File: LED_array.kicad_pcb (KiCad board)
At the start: 4 copper layers, 40 x 48 mm, 135 parts, among them J1 5040500691

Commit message: uodate 5/4/2021
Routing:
- net +5VD: track 109.7 -> 108.4 mm
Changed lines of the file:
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@@
     (thickness 1.6)
     (drawings 14)
-    (tracks 732)
+    (tracks 730)
     (zones 0)
     (modules 135)
@@
   (layers
     (0 F.Cu signal)
-    (1 In1.Cu power)
-    (2 In2.Cu signal)
+    (1 In1.Cu power hide)
+    (2 In2.Cu signal hide)
     (31 B.Cu power)
-    (32 B.Adhes user)
-    (33 F.Adhes user)
-    (34 B.Paste user)
-    (35 F.Paste user)
-    (36 B.SilkS user)
-    (37 F.SilkS user)
-    (38 B.Mask user)
-    (39 F.Mask user)
-    (40 Dwgs.User user)
-    (41 Cmts.User user)
-    (42 Eco1.User user)
-    (43 Eco2.User user)
-    (44 Edge.Cuts user)
-    (45 Margin user)
-    (46 B.CrtYd user)
-    (47 F.CrtYd user)
+    (32 B.Adhes user hide)
+    (33 F.Adhes user hide)
+    (34 B.Paste user hide)
+    (35 F.Paste user hide)
+    (36 B.SilkS user hide)
+    (37 F.SilkS user hide)
+    (38 B.Mask user hide)
+    (39 F.Mask user hide)
+    (40 Dwgs.User user hide)
+    (41 Cmts.User user hide)
+    (42 Eco1.User user hide)
+    (43 Eco2.User user hide)
+    (44 Edge.Cuts user hide)
+    (45 Margin user hide)
+    (46 B.CrtYd user hide)
+    (47 F.CrtYd user hide)
     (48 B.Fab user hide)
     (49 F.Fab user hide)
@@
       (effects (font (size 1 1) (thickness 0.015)))
     )
-    (fp_text user 1.50mm~Pitch,~Pico-Lock~PCB~Header,~Single~Row,~Right-Angle (at -10.5 5) (layer F.Fab)
-      (effects (font (size 0.393701 0.393701) (thickness 0.015)))
-    )
     (fp_poly (pts (xy -7.8762 -0.5762) (xy -7.1238 -0.5762) (xy -7.1238 0.5762) (xy -7.8762 0.5762)) (layer F.Mask) (width 0.01))
     (fp_poly (pts (xy -6.3762 -0.5762) (xy -5.6238 -0.5762) (xy -5.6238 0.5762) (xy -6.3762 0.5762)) (layer F.Mask) (width 0.01))
@@
     (fp_line (start 4.295 -7.36) (end 4.295 1.62) (layer F.CrtYd) (width 0.05))
     (fp_line (start -11.795 -7.36) (end 4.295 -7.36) (layer F.CrtYd) (width 0.05))
+    (fp_text user 1.50mm~Pitch,~Pico-Lock~PCB~Header,~Single~Row,~Right-Angle (at -10.5 5) (layer F.Fab)
+      (effects (font (size 0.393701 0.393701) (thickness 0.015)))
+    )
     (pad S1 smd rect (at 2.605 -5.19) (size 1.25 1.8) (layers F.Cu F.Paste))
     (pad 6 smd rect (at -7.5 0.3) (size 0.6 1.6) (layers F.Cu F.Paste)
@@
       (effects (font (size 0.5 0.5) (thickness 0.1)))
     )
-    (fp_text user %R (at 0 0 180) (layer F.Fab)
-      (effects (font (size 0.3 0.3) (thickness 0.07)))
-    )
     (fp_line (start -1.025 1.025) (end 1.025 1.025) (layer F.CrtYd) (width 0.05))
     (fp_line (start -1 -1) (end 1 -1) (layer F.Fab) (width 0.1))
@@
     (fp_line (start -1.025 -1.025) (end -1.025 1.025) (layer F.CrtYd) (width 0.05))
     (fp_line (start -1.025 -1.025) (end 1.025 -1.025) (layer F.CrtYd) (width 0.05))
+    (fp_text user %R (at 0 0 180) (layer F.Fab)
+      (effects (font (size 0.3 0.3) (thickness 0.07)))
+    )
     (pad 4 smd rect (at -0.8 -0.7 180) (size 0.45 0.65) (layers F.Cu F.Paste F.Mask)
       (net 11 "Net-(D127-Pad3)"))
@@
   (via (at 71.7 57.8) (size 0.4) (drill 0.2) (layers F.Cu B.Cu) (net 2))
   (via (at 74.3 57.8) (size 0.4) (drill 0.2) (layers F.Cu B.Cu) (net 2))
-  (segment (start 54.69 47.41) (end 54.75 47.47) (width 0.3) (layer B.Cu) (net 2))
-  (segment (start 53.5 47.41) (end 54.69 47.41) (width 0.3) (layer B.Cu) (net 2))
   (segment (start 56.61 29.74) (end 56.61 28.21) (width 0.8) (layer F.Cu) (net 2))
+  (via (at 76 29.6) (size 0.8) (drill 0.4) (layers F.Cu B.Cu) (net 2))
+  (via (at 72 29.6) (size 0.8) (drill 0.4) (layers F.Cu B.Cu) (net 2))
+  (via (at 48.6 29.6) (size 0.8) (drill 0.4) (layers F.Cu B.Cu) (net 2))
+  (via (at 44.6 29.6) (size 0.8) (drill 0.4) (layers F.Cu B.Cu) (net 2))
+  (segment (start 44.6 28.475) (end 44.6 29.6) (width 0.8) (layer F.Cu) (net 2))
+  (segment (start 48.6 29.6) (end 48.6 28.475) (width 0.8) (layer F.Cu) (net 2))
+  (segment (start 72 29.6) (end 72 28.475) (width 0.8) (layer F.Cu) (net 2))
+  (segment (start 76 28.475) (end 76 29.6) (width 0.8) (layer F.Cu) (net 2))
   (segment (start 51.321818 33.34501) (end 50.1 34.566828) (width 0.2) (layer F.Cu) (net 3))
   (segment (start 50.1 34.566828) (end 50.1 35) (width 0.2) (layer F.Cu) (net 3))
@@
   (segment (start 59.61 32.205) (end 59.245 32.57) (width 0.25) (layer F.Cu) (net 260))
   (segment (start 59.61 29.74) (end 59.61 32.205) (width 0.25) (layer F.Cu) (net 260))
-  (via (at 76 29.6) (size 0.8) (drill 0.4) (layers F.Cu B.Cu) (net 2))
-  (via (at 72 29.6) (size 0.8) (drill 0.4) (layers F.Cu B.Cu) (net 2))
-  (via (at 48.6 29.6) (size 0.8) (drill 0.4) (layers F.Cu B.Cu) (net 2))
-  (via (at 44.6 29.6) (size 0.8) (drill 0.4) (layers F.Cu B.Cu) (net 2))
-  (segment (start 44.6 28.475) (end 44.6 29.6) (width 0.8) (layer F.Cu) (net 2))
-  (segment (start 48.6 29.6) (end 48.6 28.475) (width 0.8) (layer F.Cu) (net 2))
-  (segment (start 72 29.6) (end 72 28.475) (width 0.8) (layer F.Cu) (net 2))
-  (segment (start 76 28.475) (end 76 29.6) (width 0.8) (layer F.Cu) (net 2))
   (zone (net 2) (net_name +5VD) (layer In1.Cu) (hatch edge 0.508)
     (connect_pads (clearance 0.508))
@@
       )
     )
-  )
-  (zone (net 0) (net_name "") (layer B.Cu) (hatch edge 0.508)
-    (connect_pads (clearance 0.508))
-    (min_thickness 0.254)
-    (keepout (tracks allowed) (vias allowed) (copperpour not_allowed))
-    (fill (arc_segments 32) (thermal_gap 0.508) (thermal_bridge_width 0.508))
-    (polygon
-      (pts
-        (xy 65.87 48.1) (xy 64.5 48.08) (xy 64.44 46.52) (xy 64.44 46.5) (xy 65.82 46.5)
-      )
-    )

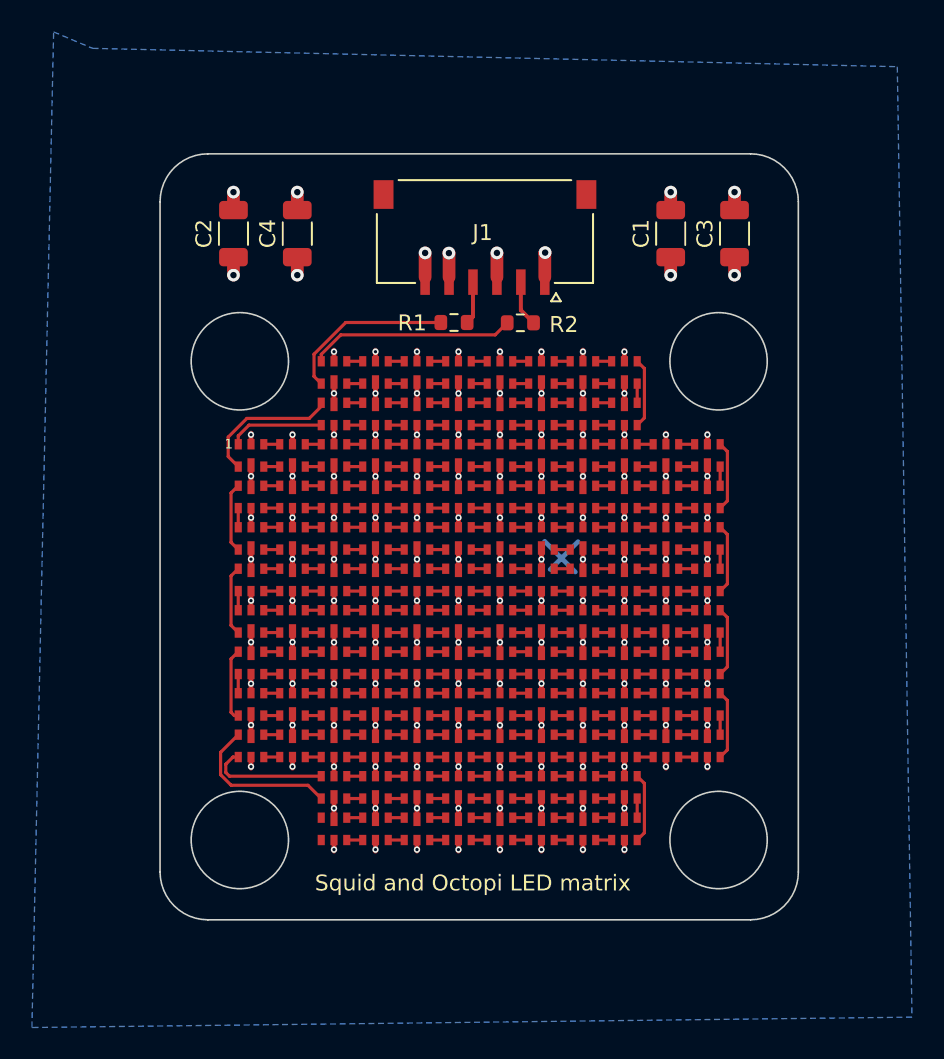
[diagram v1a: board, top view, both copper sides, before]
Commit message: v2 - add a USB-C connector
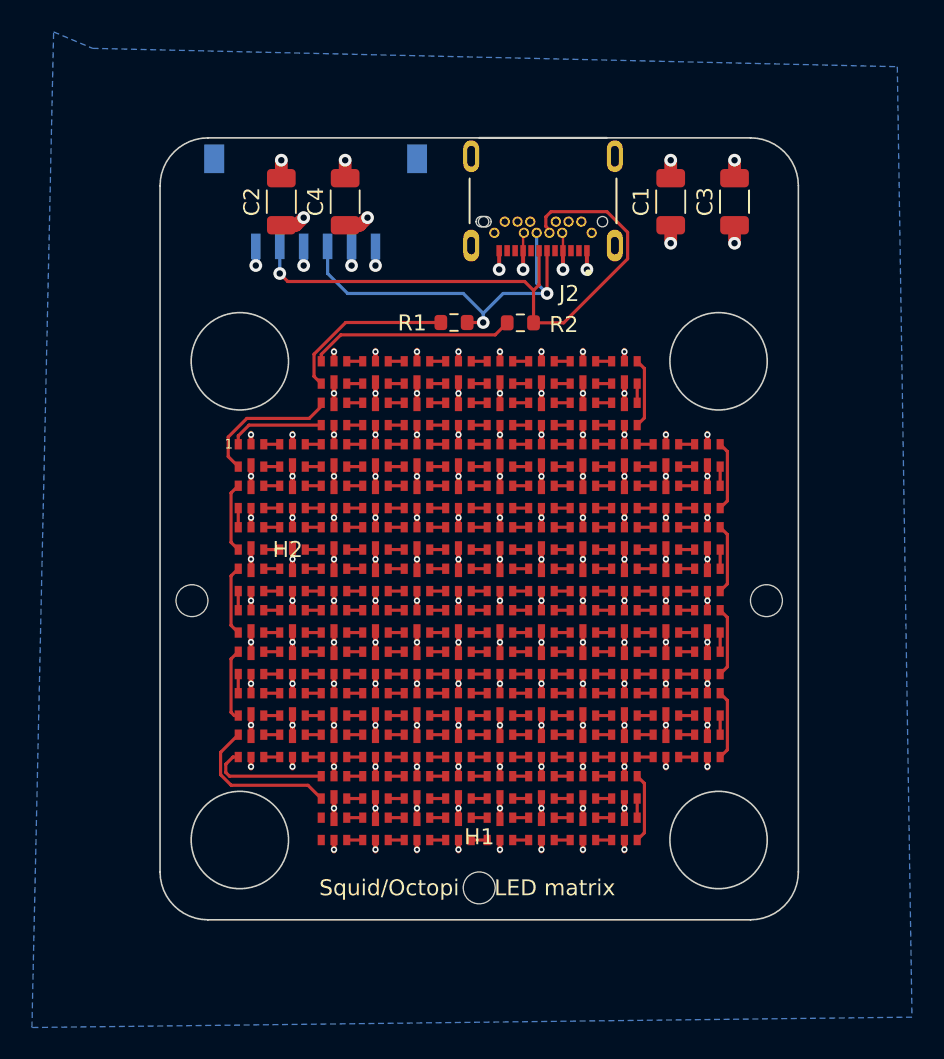
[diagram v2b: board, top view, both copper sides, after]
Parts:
- added H1: MountingHole, MountingHole:MountingHole_2mm, F.Cu at (60.0, 68.0)
- added H2: MountingHole, MountingHole:MountingHole_2mm, F.Cu at (48.0, 50.0)
- added H3: MountingHole, MountingHole:MountingHole_2mm, F.Cu at (95.3, 48.0)
- added J2: USB4055-30-A, Connector:GCT_USB4055-30-A, F.Cu at (64.0, 23.5)
- J1: moved to B.Cu
- moved J1 18.2 mm to (46.0, 27.5), turned to 180 degrees
- moved C2 3.61 mm to (47.6, 25.0)
- moved C4 3.61 mm to (51.6, 25.0)
- moved C1 2.00 mm to (72.0, 25.0)
- moved C3 2.00 mm to (76.0, 25.0)
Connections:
- net Net-(J1-Pad2) renamed /sdi
- net Net-(J1-Pad4) renamed /cki
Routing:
- net /sdi: track 3.18 -> 38.8 mm, vias 0 -> 1
- net /cki: track 2.98 -> 25.3 mm, vias 0 -> 2
- net +5VD: track 108.4 -> 113.7 mm, vias 69 -> 71
- net GND: track 103.9 -> 100.1 mm, vias 83 -> 85
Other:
- board size 40 x 48 mm -> 40 x 49 mm
- board text added: "Squid/Octopi LED matrix"
- board text added: "by RB & HL Prakash Lab, Stanford University v1: 04/12/2021 v2: 03/05/2022"
- board text removed: "Designed by Rinni Bhansali With minor edits from Hongquan Li Prakash Lab, Stanford University 04/12/2021"
- board text removed: "Squid and Octopi LED matrix"
